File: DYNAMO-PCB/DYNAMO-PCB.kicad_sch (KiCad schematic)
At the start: 14 parts, among them J13 Conn_01x02_Pin, J18 USB3_A, J20 HDMI_A, J21 USB3_A, J22 USB3_A, J23 USB3_A, J24 USB3_A, J25 USB3_A, J27 HDMI_A, J3 Conn_01x03_Pin, J34 Conn_02x05_Counter_Clockwise

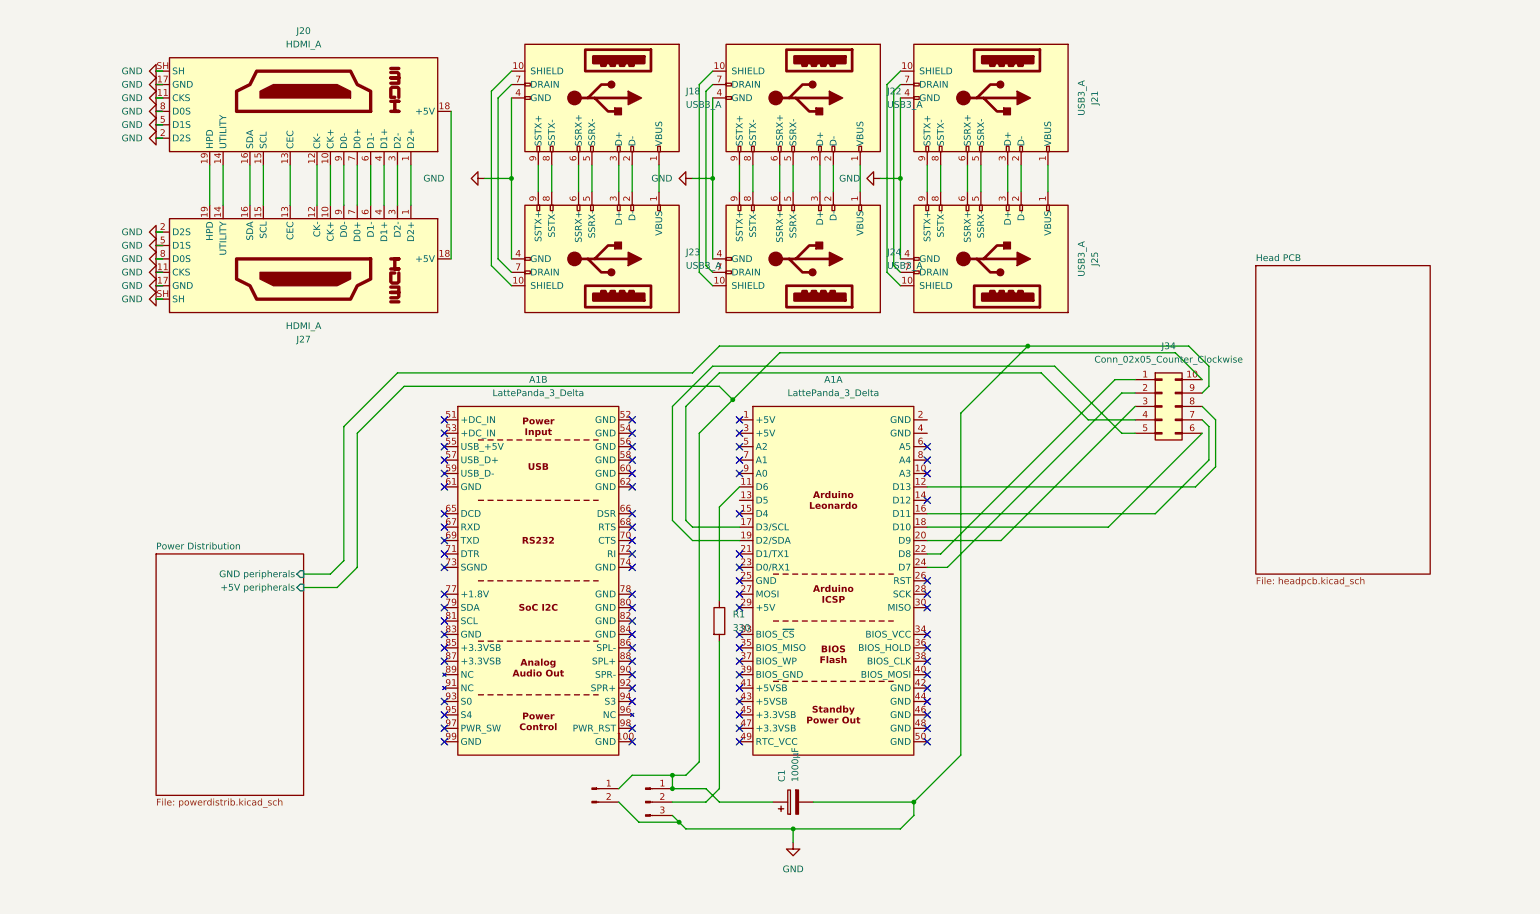
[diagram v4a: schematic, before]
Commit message: fix erc errors
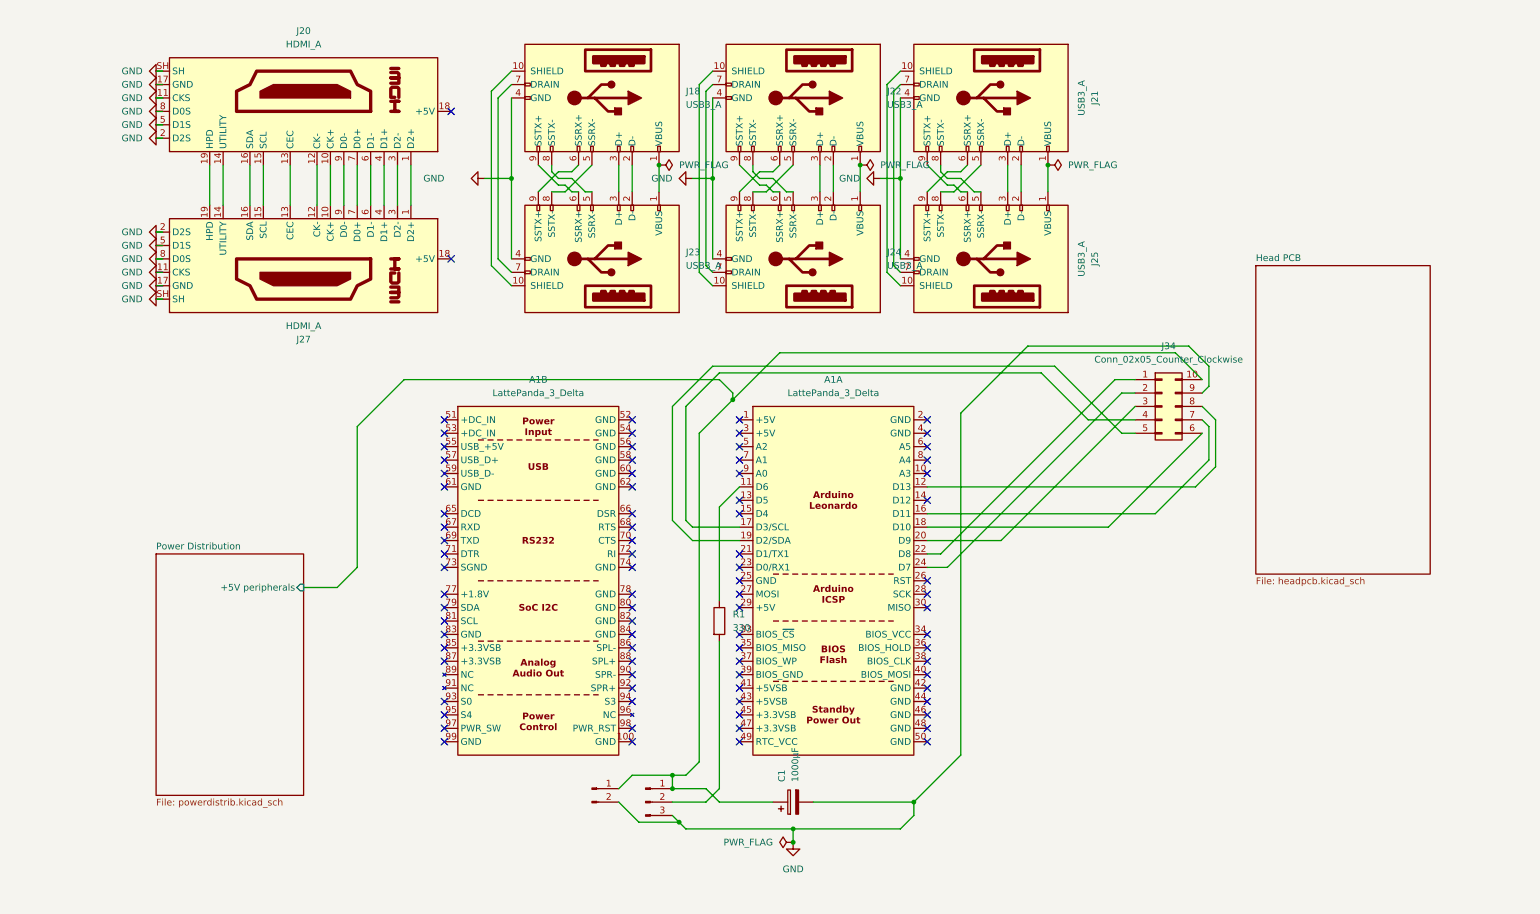
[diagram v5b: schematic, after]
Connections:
- net at J24.5 (SSRX-): now also J22.8 (SSTX-); no longer J22.5 (SSRX-)
- net at J24.6 (SSRX+): now also J22.9 (SSTX+); no longer J22.6 (SSRX+)
- net at J24.8 (SSTX-): now also J22.5 (SSRX-); no longer J22.8 (SSTX-)
- net at J24.9 (SSTX+): now also J22.6 (SSRX+); no longer J22.9 (SSTX+)
- net at J21.5 (SSRX-): now also J25.8 (SSTX-); no longer J25.5 (SSRX-)
- net at J21.6 (SSRX+): now also J25.9 (SSTX+); no longer J25.6 (SSRX+)
- net at J21.8 (SSTX-): now also J25.5 (SSRX-); no longer J25.8 (SSTX-)
- net at J21.9 (SSTX+): now also J25.6 (SSRX+); no longer J25.9 (SSTX+)
- net at J18.5 (SSRX-): now also J23.8 (SSTX-); no longer J23.5 (SSRX-)
- net at J18.6 (SSRX+): now also J23.9 (SSTX+); no longer J23.6 (SSRX+)
- net at J18.8 (SSTX-): now also J23.5 (SSRX-); no longer J23.8 (SSTX-)
- net at J18.9 (SSTX+): now also J23.6 (SSRX+); no longer J23.9 (SSTX+)
- net at J27.18 (+5V): no longer J20.18 (+5V)
- no-connect marks 79 -> 84
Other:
- sheet Power Distribution ports: added none; removed GND peripherals

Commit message: placement wip
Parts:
- added J29, J30: HDMI_A, Connector_Video:HDMI_A_Molex_208658-1001_Horizontal, symbol Connector:HDMI_A
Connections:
- net GND: now also J29.11 (CKS), J29.17 (GND), J29.2 (D2S), J29.5 (D1S), J29.8 (D0S), J29.SH, J30.11 (CKS), J30.17 (GND), J30.2 (D2S), J30.5 (D1S), J30.8 (D0S), J30.SH
- new net: J29.1 (D2+), J30.1 (D2+)
- new net: J29.10 (CK+), J30.10 (CK+)
- new net: J29.12 (CK-), J30.12 (CK-)
- new net: J29.13 (CEC), J30.13 (CEC)
- new net: J29.14 (UTILITY), J30.14 (UTILITY)
- new net: J29.15 (SCL), J30.15 (SCL)
- new net: J29.16 (SDA), J30.16 (SDA)
- new net: J29.19 (HPD), J30.19 (HPD)
- new net: J29.3 (D2-), J30.3 (D2-)
- new net: J29.4 (D1+), J30.4 (D1+)
- new net: J29.6 (D1-), J30.6 (D1-)
- new net: J29.7 (D0+), J30.7 (D0+)
- new net: J29.9 (D0-), J30.9 (D0-)
- no-connect marks 84 -> 86
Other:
- moved on the sheet: J18, J21, J22, J23, J24, J25

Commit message: headphone jack
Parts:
- added J1, J16: SJ1-3533NS, SJ1-3533NS:CUI_SJ1-3533NS, symbol SJ1-3533NS:SJ1-3533NS
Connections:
- new net: J1.1, J16.1
- new net: J1.2, J16.2
- new net: J1.3, J16.3
- new net: J1.SH1 (SHIELD), J1.SH2 (SHIELD), J1.SH3 (SHIELD), J16.SH1 (SHIELD), J16.SH2 (SHIELD), J16.SH3 (SHIELD)
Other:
- moved on the sheet: J18, J20, J21, J22, J23, J24, J25, J27, J29, J30

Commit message: routing
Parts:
- renumbered J18 to Camera1, J23 to Camera2, J13 to CentralFan1, J3 to CentralLEDs1, J20 to Display_A1, J27 to Display_A2, J29 to Display_B1, J30 to Display_B2, J34 to HeadFlat1, J22 to Microphone1, J24 to Microphone2, J21 to Misc1, J25 to Misc2, J16 to Speaker1, J1 to Speaker2
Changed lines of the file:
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@@
 		(on_board yes)
 		(dnp no)
-		(property "Reference" "J24"
+		(property "Reference" "Microphone2"
 			(at 245.11 57.1499 90)
 			(effects
@@
 			(project "DYNAMO-PCB"
 				(path "/2ca9dd43-411d-4cc5-8a4b-ed00d72bae91"
-					(reference "J24")
+					(reference "Microphone2")
 					(unit 1)
 				)
@@
 		(on_board yes)
 		(dnp no)
-		(property "Reference" "J21"
+		(property "Reference" "Misc1"
 			(at 284.48 27.94 0)
 			(effects
@@
 			(project "DYNAMO-PCB"
 				(path "/2ca9dd43-411d-4cc5-8a4b-ed00d72bae91"
-					(reference "J21")
+					(reference "Misc1")
 					(unit 1)
 				)
@@
 		(on_board yes)
 		(dnp no)
-		(property "Reference" "J3"
+		(property "Reference" "CentralLEDs1"
 			(at 118.11 162.56 90)
 			(effects
@@
 			(project ""
 				(path "/2ca9dd43-411d-4cc5-8a4b-ed00d72bae91"
-					(reference "J3")
+					(reference "CentralLEDs1")
 					(unit 1)
 				)
@@
 		(on_board yes)
 		(dnp no)
-		(property "Reference" "J29"
+		(property "Reference" "Display_B1"
 			(at 139.7 13.97 90)
 			(effects
@@
 			(project "DYNAMO-PCB"
 				(path "/2ca9dd43-411d-4cc5-8a4b-ed00d72bae91"
-					(reference "J29")
+					(reference "Display_B1")
 					(unit 1)
 				)
@@
 		(on_board yes)
 		(dnp no)
-		(property "Reference" "J13"
+		(property "Reference" "CentralFan1"
 			(at 114.9351 163.83 90)
 			(effects
@@
 			(project "DYNAMO-PCB"
 				(path "/2ca9dd43-411d-4cc5-8a4b-ed00d72bae91"
-					(reference "J13")
+					(reference "CentralFan1")
 					(unit 1)
 				)
@@
 		(dnp no)
 		(fields_autoplaced yes)
-		(property "Reference" "J18"
+		(property "Reference" "Camera1"
 			(at 207.01 26.6699 90)
 			(effects
@@
 			(project "DYNAMO-PCB"
 				(path "/2ca9dd43-411d-4cc5-8a4b-ed00d72bae91"
-					(reference "J18")
+					(reference "Camera1")
 					(unit 1)
 				)
@@
 		(on_board yes)
 		(dnp no)
-		(property "Reference" "J25"
+		(property "Reference" "Misc2"
 			(at 284.48 58.42 0)
 			(effects
@@
 			(project "DYNAMO-PCB"
 				(path "/2ca9dd43-411d-4cc5-8a4b-ed00d72bae91"
-					(reference "J25")
+					(reference "Misc2")
 					(unit 1)
 				)
@@
 		(dnp no)
 		(fields_autoplaced yes)
-		(property "Reference" "J34"
+		(property "Reference" "HeadFlat1"
 			(at 222.25 76.2 0)
 			(effects
@@
 			(project "DYNAMO-PCB"
 				(path "/2ca9dd43-411d-4cc5-8a4b-ed00d72bae91"
-					(reference "J34")
+					(reference "HeadFlat1")
 					(unit 1)
 				)
@@
 		(on_board yes)
 		(dnp no)
-		(property "Reference" "J16"
+		(property "Reference" "Speaker1"
 			(at 16.51 26.6699 90)
 			(effects
@@
 			(project ""
 				(path "/2ca9dd43-411d-4cc5-8a4b-ed00d72bae91"
-					(reference "J16")
+					(reference "Speaker1")
 					(unit 1)
 				)
@@
 		(dnp no)
 		(fields_autoplaced yes)
-		(property "Reference" "J1"
+		(property "Reference" "Speaker2"
 			(at 39.37 57.1499 90)
 			(effects
@@
 			(project ""
 				(path "/2ca9dd43-411d-4cc5-8a4b-ed00d72bae91"
-					(reference "J1")
+					(reference "Speaker2")
 					(unit 1)
 				)
@@
 		(on_board yes)
 		(dnp no)
-		(property "Reference" "J30"
+		(property "Reference" "Display_B2"
 			(at 139.7 72.39 90)
 			(effects
@@
 			(project "DYNAMO-PCB"
 				(path "/2ca9dd43-411d-4cc5-8a4b-ed00d72bae91"
-					(reference "J30")
+					(reference "Display_B2")
 					(unit 1)
 				)
@@
 		(on_board yes)
 		(dnp no)
-		(property "Reference" "J27"
+		(property "Reference" "Display_A2"
 			(at 76.2 72.39 90)
 			(effects
@@
 			(project "DYNAMO-PCB"
 				(path "/2ca9dd43-411d-4cc5-8a4b-ed00d72bae91"
-					(reference "J27")
+					(reference "Display_A2")
 					(unit 1)
 				)
@@
 		(on_board yes)
 		(dnp no)
-		(property "Reference" "J23"
+		(property "Reference" "Camera2"
 			(at 207.01 57.1499 90)
 			(effects
@@
 			(project "DYNAMO-PCB"
 				(path "/2ca9dd43-411d-4cc5-8a4b-ed00d72bae91"
-					(reference "J23")
+					(reference "Camera2")
 					(unit 1)
 				)
@@
 		(on_board yes)
 		(dnp no)
-		(property "Reference" "J22"
+		(property "Reference" "Microphone1"
 			(at 245.11 26.6699 90)
 			(effects
@@
 			(project "DYNAMO-PCB"
 				(path "/2ca9dd43-411d-4cc5-8a4b-ed00d72bae91"
-					(reference "J22")
+					(reference "Microphone1")
 					(unit 1)
 				)
@@
 		(on_board yes)
 		(dnp no)
-		(property "Reference" "J20"
+		(property "Reference" "Display_A1"
 			(at 76.2 13.97 90)
 			(effects
@@
 			(project "DYNAMO-PCB"
 				(path "/2ca9dd43-411d-4cc5-8a4b-ed00d72bae91"
-					(reference "J20")
+					(reference "Display_A1")
 					(unit 1)
 				)
